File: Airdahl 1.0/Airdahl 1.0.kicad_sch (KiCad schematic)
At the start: 26 parts, among them J1 Conn_ARM_JTAG_SWD_20, SW1 SW_MEC_5E, U1 STM32F446RETx, X2 ABS25-32.768KHZ-6-T, Y1 ABM3B-8.000MHZ-12-D1X-T

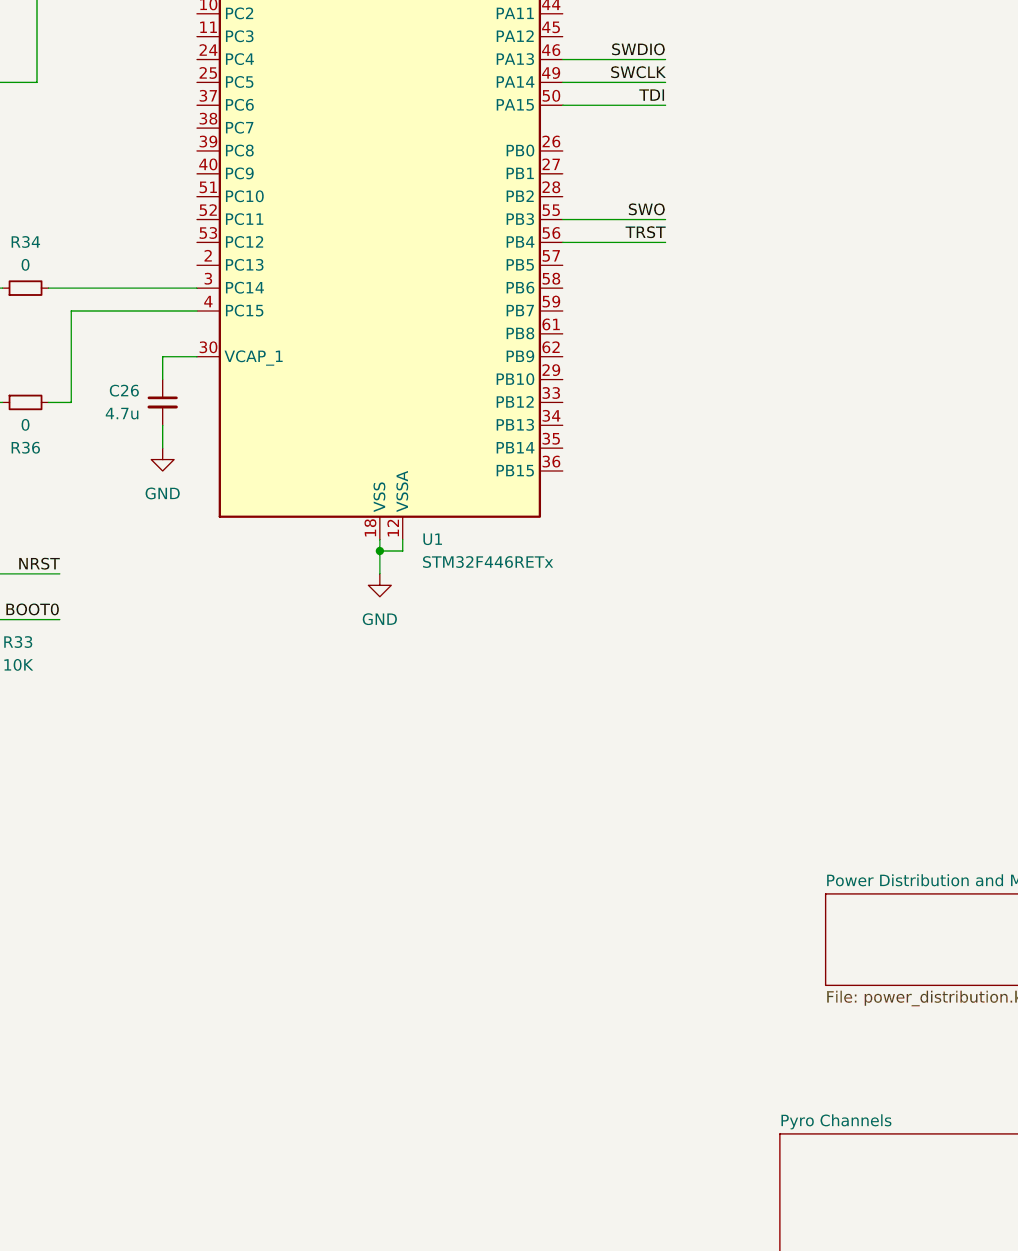
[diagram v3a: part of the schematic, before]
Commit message: basic i2c setup
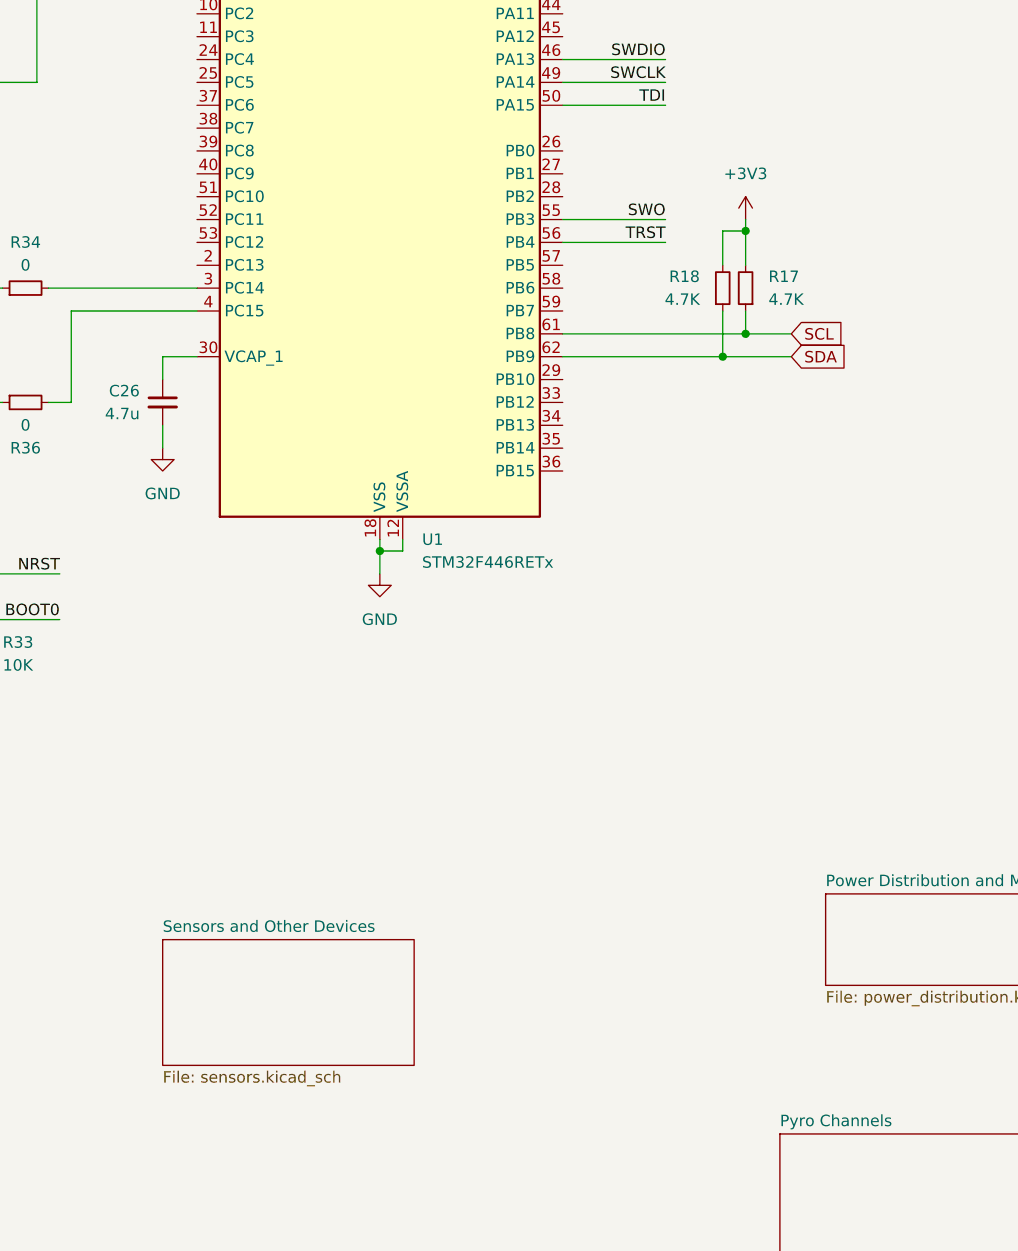
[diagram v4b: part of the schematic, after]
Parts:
- added R17, R18: 4.7K, Resistor_SMD:R_0201_0603Metric_Pad0.64x0.40mm_HandSolder, symbol Device:R_Small
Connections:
- net +3V3: now also R17.2, R18.2
- net SCL: now reaches U1.61 (PB8)
- net SCL: now also R17.1
- net SDA: now reaches U1.62 (PB9)
- net SDA: now also R18.1
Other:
- added sheet Sensors and Other Devices (sensors.kicad_sch)

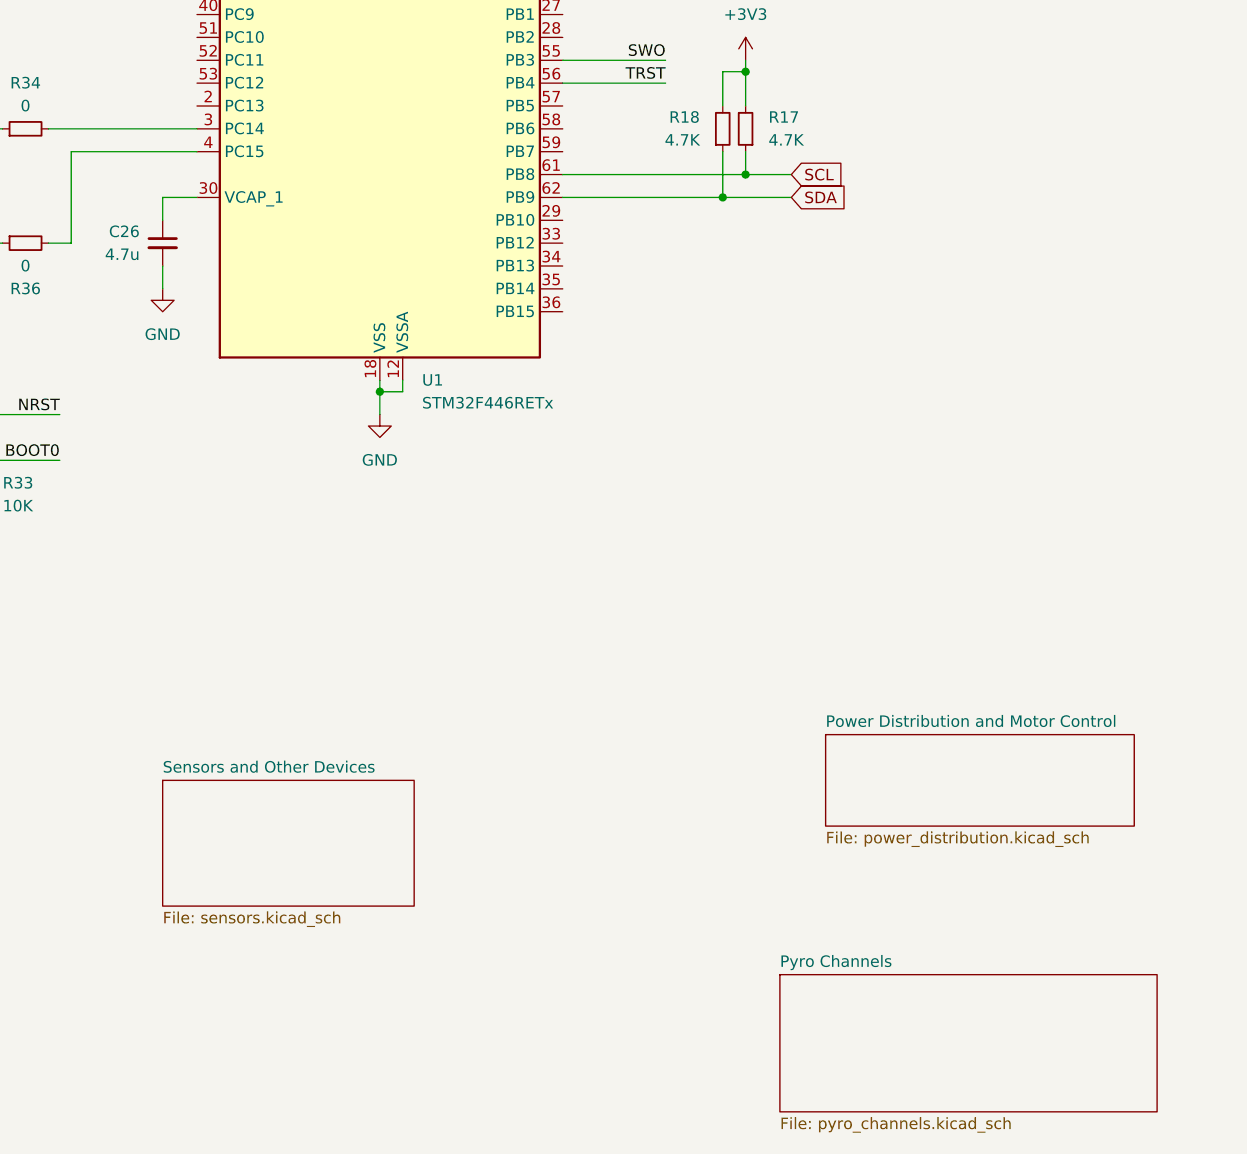
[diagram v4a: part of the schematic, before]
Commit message: wired up dat ho (sitting on int/rst signals until we figure out rest of gpio)
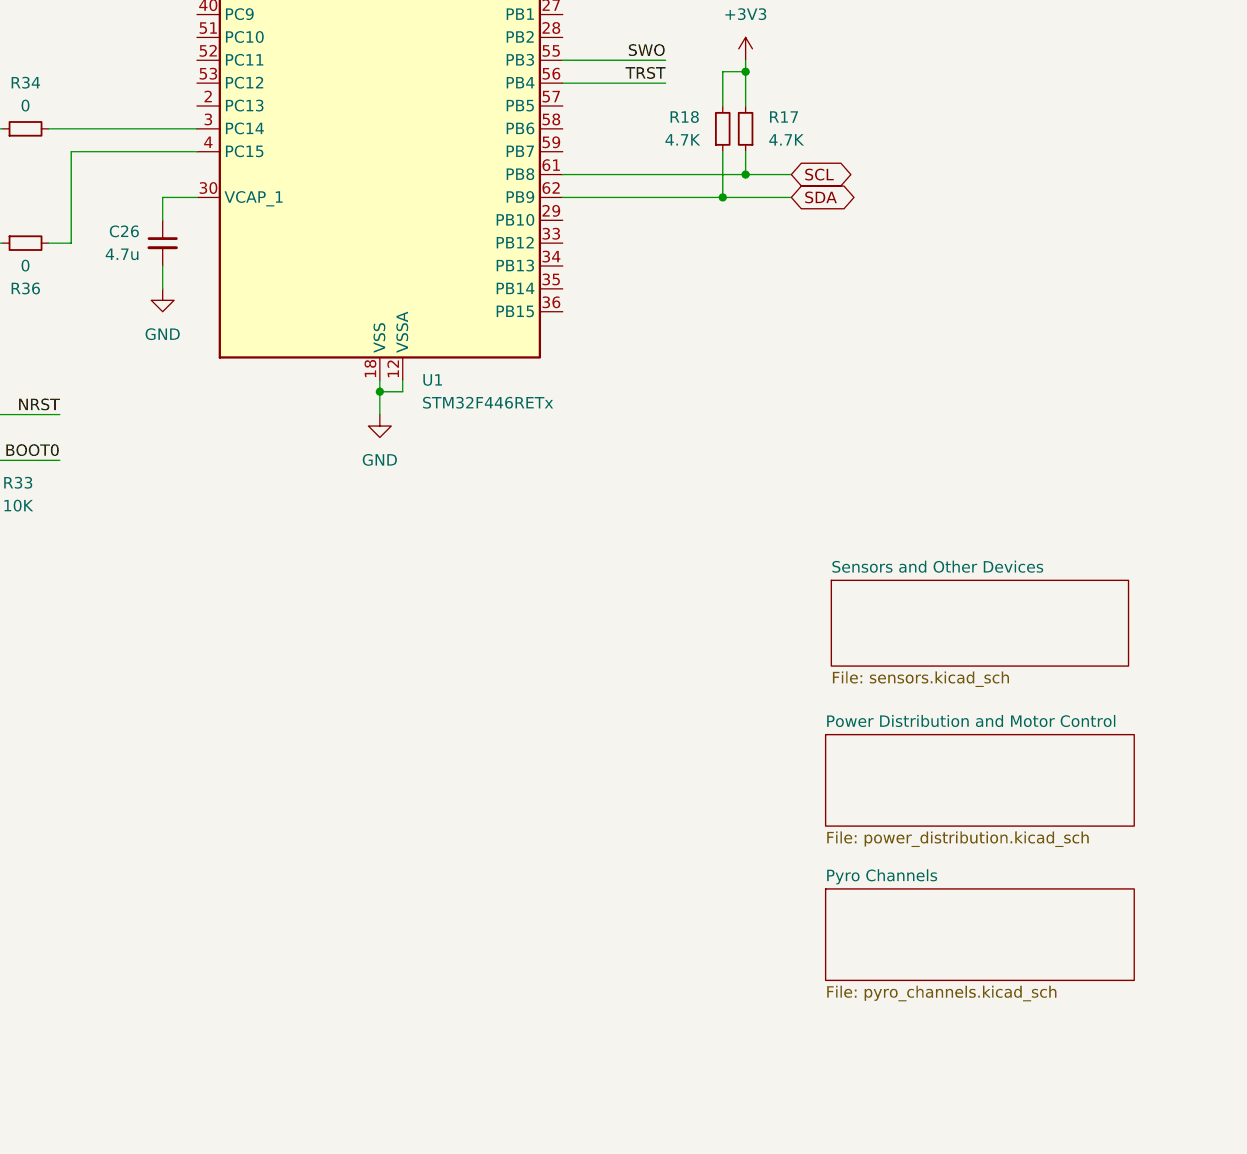
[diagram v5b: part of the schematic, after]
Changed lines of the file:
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@@
 	)
 	(global_label "SDA"
-		(shape input)
+		(shape bidirectional)
 		(at 241.3 158.75 0)
 		(fields_autoplaced yes)
@@
 		)
 		(property "Intersheetrefs" "${INTERSHEET_REFS}"
-			(at 247.8533 158.75 0)
+			(at 248.9646 158.75 0)
 			(effects
 				(font
@@
 	)
 	(global_label "SCL"
-		(shape input)
+		(shape bidirectional)
 		(at 241.3 156.21 0)
 		(fields_autoplaced yes)
@@
 		)
 		(property "Intersheetrefs" "${INTERSHEET_REFS}"
-			(at 247.7928 156.21 0)
+			(at 248.9041 156.21 0)
 			(effects
 				(font
@@
 	)
 	(sheet
-		(at 240.03 245.11)
-		(size 41.91 15.24)
+		(at 245.11 235.585)
+		(size 34.29 10.16)
 		(exclude_from_sim no)
 		(in_bom yes)
@@
 		)
 		(property "Sheetname" "Pyro Channels"
-			(at 240.03 244.3984 0)
+			(at 245.11 234.8734 0)
 			(effects
 				(font
@@
 		)
 		(property "Sheetfile" "pyro_channels.kicad_sch"
-			(at 240.03 260.9346 0)
+			(at 245.11 246.3296 0)
 			(effects
 				(font
@@
 	)
 	(sheet
-		(at 171.45 223.52)
-		(size 27.94 13.97)
+		(at 245.745 201.295)
+		(size 33.02 9.525)
 		(exclude_from_sim no)
 		(in_bom yes)
@@
 		)
 		(property "Sheetname" "Sensors and Other Devices"
-			(at 171.45 222.8084 0)
+			(at 245.745 200.5834 0)
 			(effects
 				(font
@@
 		)
 		(property "Sheetfile" "sensors.kicad_sch"
-			(at 171.45 238.0746 0)
+			(at 245.745 211.4046 0)
 			(effects
 				(font

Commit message: rfm wiring
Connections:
- net CS_RFM: now reaches U1.20 (PA4)
- net SCLK: now reaches U1.21 (PA5)
- net MISO: now reaches U1.22 (PA6)
- net MOSI: now reaches U1.23 (PA7)
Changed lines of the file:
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@@
+	(wire
+		(pts
+			(xy 215.9 110.49) (xy 218.44 110.49)
+		)
+		(stroke
+			(width 0)
+			(type default)
+		)
+	)
 	(wire
 		(pts
@@
 	(wire
 		(pts
+			(xy 215.9 107.95) (xy 218.44 107.95)
+		)
+		(stroke
+			(width 0)
+			(type default)
+		)
+	)
+	(wire
+		(pts
 			(xy 135.89 187.96) (xy 135.89 185.42)
 		)
@@
 	(wire
 		(pts
+			(xy 215.9 102.87) (xy 218.44 102.87)
+		)
+		(stroke
+			(width 0)
+			(type default)
+		)
+	)
+	(wire
+		(pts
 			(xy 226.06 82.55) (xy 226.06 85.09)
 		)
@@
 		(pts
 			(xy 135.89 151.13) (xy 144.78 151.13)
+		)
+		(stroke
+			(width 0)
+			(type default)
+		)
+	)
+	(wire
+		(pts
+			(xy 215.9 105.41) (xy 218.44 105.41)
 		)
 		(stroke
@@
 			(effects
 				(font
+					(size 1.27 1.27)
+				)
+				(justify left)
+				(hide yes)
+			)
+		)
+	)
+	(global_label "SCLK"
+		(shape bidirectional)
+		(at 218.44 105.41 0)
+		(fields_autoplaced yes)
+		(effects
+			(font
+				(size 1.27 1.27)
+			)
+			(justify left)
+		)
+		(property "Intersheetrefs" "${INTERSHEET_REFS}"
+			(at 227.3141 105.41 0)
+			(effects
+				(font
+					(size 1.27 1.27)
+				)
+				(justify left)
+				(hide yes)
+			)
+		)
+	)
+	(global_label "CS_RFM"
+		(shape bidirectional)
+		(at 218.44 102.87 0)
+		(fields_autoplaced yes)
+		(effects
+			(font
+				(size 1.27 1.27)
+			)
+			(justify left)
+		)
+		(property "Intersheetrefs" "${INTERSHEET_REFS}"
+			(at 229.7936 102.87 0)
+			(effects
+				(font
+					(size 1.27 1.27)
+				)
+				(justify left)
+				(hide yes)
+			)
+		)
+	)
+	(global_label "MOSI"
+		(shape bidirectional)
+		(at 218.44 110.49 0)
+		(fields_autoplaced yes)
+		(effects
+			(font
+				(size 1.27 1.27)
+			)
+			(justify left)
+		)
+		(property "Intersheetrefs" "${INTERSHEET_REFS}"
+			(at 227.1327 110.49 0)
+			(effects
+				(font
+					(size 1.27 1.27)
+				)
+				(justify left)
+				(hide yes)
+			)
+		)
+	)
+	(global_label "MISO"
+		(shape bidirectional)
+		(at 218.44 107.95 0)
+		(fields_autoplaced yes)
+		(effects
+			(font
+				(size 1.27 1.27)
+			)
+			(justify left)
+		)
+		(property "Intersheetrefs" "${INTERSHEET_REFS}"
+			(at 227.1327 107.95 0)
+			(effects
+				(font

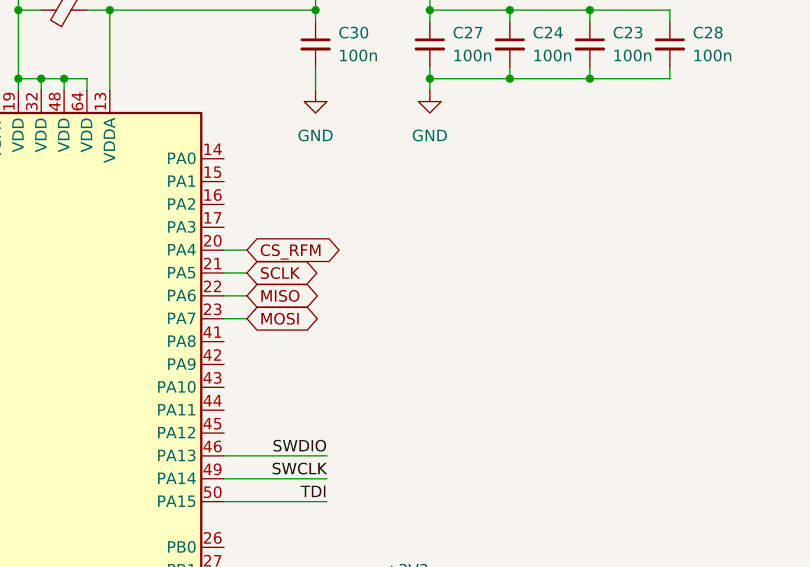
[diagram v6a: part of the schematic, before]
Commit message: added 3.3V LDO, SD Card, spi breakout
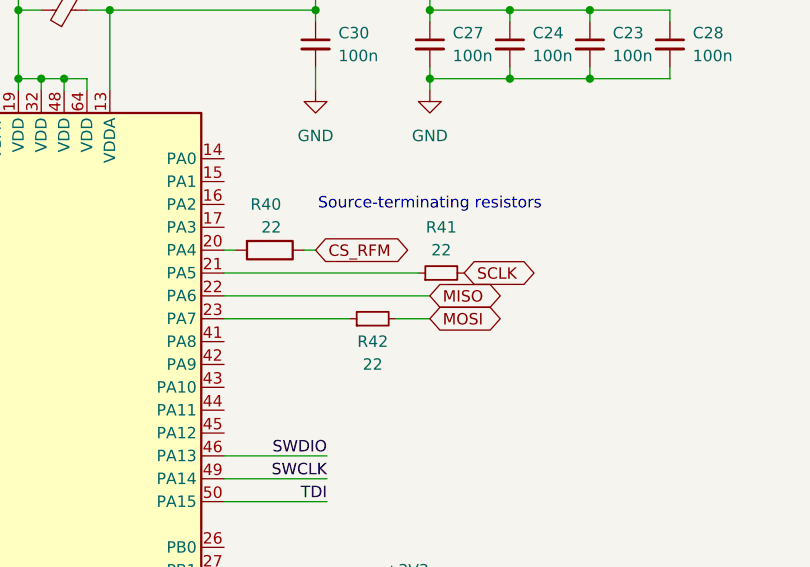
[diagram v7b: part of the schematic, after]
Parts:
- added R40: 22, Resistor_SMD:R_0402_1005Metric, symbol Device:R
- added R41, R42: 22, Resistor_SMD:R_0201_0603Metric_Pad0.64x0.40mm_HandSolder, symbol Device:R_Small
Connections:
- net CS_RFM: now also R40.1; no longer U1.20 (PA4)
- net MOSI: now also R42.2; no longer U1.23 (PA7)
- net SCLK: now also R41.2; no longer U1.21 (PA5)
- new net: R41.1, U1.21 (PA5)
- new net: R42.1, U1.23 (PA7)
- new net: R40.2, U1.20 (PA4)
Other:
- note added: "Source-terminating resistors"
